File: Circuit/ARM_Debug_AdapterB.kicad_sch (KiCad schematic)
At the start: 10 parts, among them J1 HDR-2.54 Male 2x10, J2 HDR-2.54 Male 2x7, J3 HDR-1.27 Male 2x7, J4 HDR-1.27 Male 2x5, J5 HDR-1.27 Male 2x5, J6 HDR-2.54 Male 2x6, J7 HDR-2.54 Male 1x6

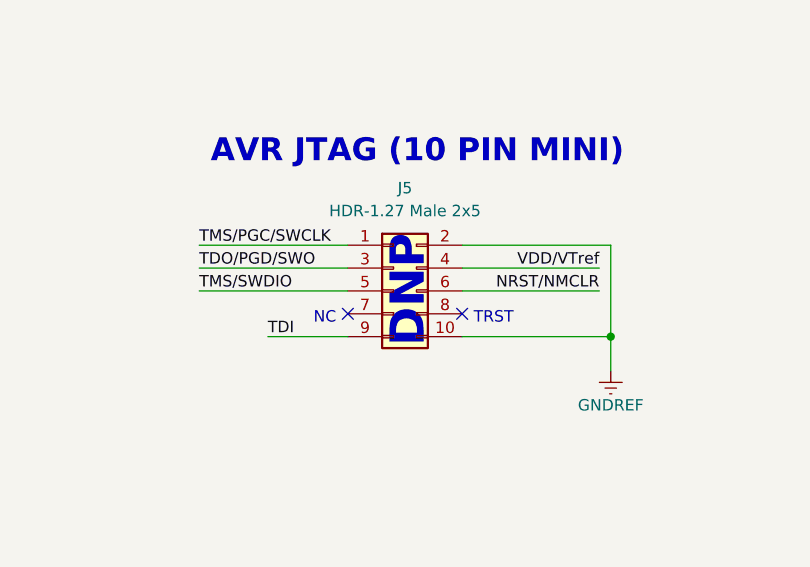
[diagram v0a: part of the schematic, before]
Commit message: Completed PCB routing
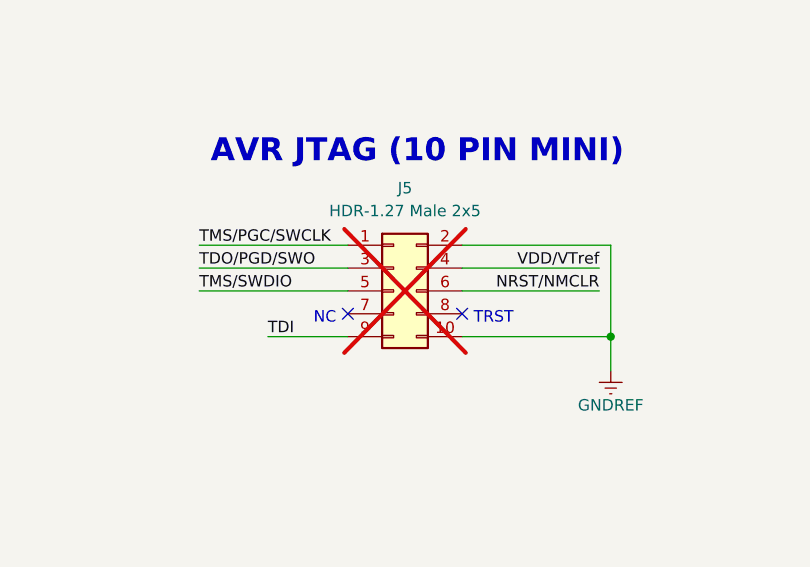
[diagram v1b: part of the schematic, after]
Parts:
- J5: now not fitted
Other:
- note removed: "DNP"
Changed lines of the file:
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@@
     (effects (font (size 1.27 1.27)) (justify left bottom))
-  )
-  (text "DNP" (at 157.48 125.73 90)
-    (effects (font (size 3.81 3.81) (thickness 0.508) bold (color 255 0 0 1)) (justify left bottom))
   )
   (text "GND_DETECT" (at 128.27 63.5 0)
@@
   )
   (symbol (lib_id "Connector_Generic:Conn_02x05_Odd_Even") (at 153.67 119.38 0) (unit 1)
-    (in_bom yes) (on_board yes) (dnp no) (fields_autoplaced)
+    (in_bom yes) (on_board yes) (dnp yes) (fields_autoplaced)
     (property "Reference" "J5" (at 154.94 107.95 0)
       (effects (font (size 1.27 1.27)))
